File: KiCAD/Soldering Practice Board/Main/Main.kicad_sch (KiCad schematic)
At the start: 1 part, among them U1 STM32C071R8Tx

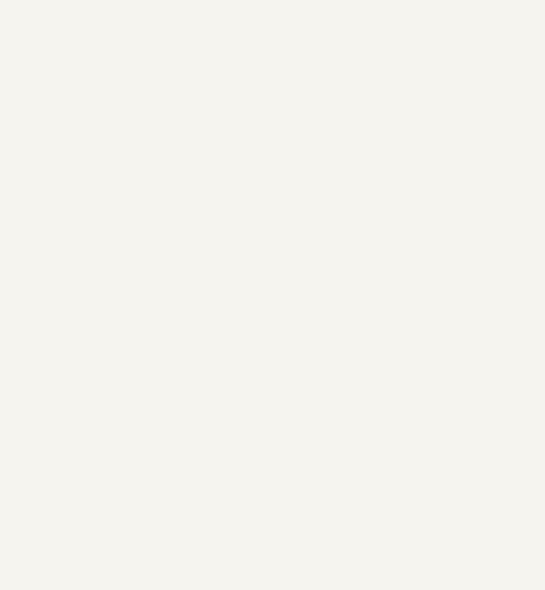
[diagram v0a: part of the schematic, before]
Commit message: Write BMi260 explanations
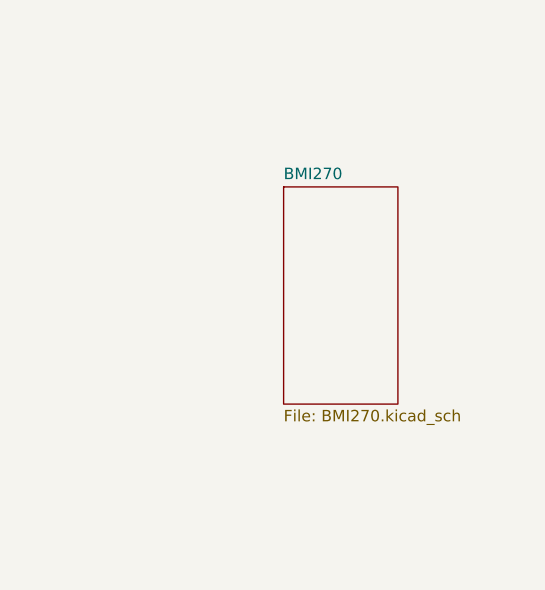
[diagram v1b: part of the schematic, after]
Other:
- added sheet BMI270 (BMI270.kicad_sch)
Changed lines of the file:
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@@
+		)
+	)
+	(sheet
+		(at 163.83 77.47)
+		(size 12.7 24.13)
+		(exclude_from_sim no)
+		(in_bom yes)
+		(on_board yes)
+		(dnp no)
+		(fields_autoplaced yes)
+		(stroke
+			(width 0.1524)
+			(type solid)
+		)
+		(fill
+			(color 0 0 0 0.0000)
+		)
+		(property "Sheetname" "BMI270"
+			(at 163.83 76.7584 0)
+			(effects
+				(font
+					(size 1.27 1.27)
+				)
+				(justify left bottom)
+			)
+		)
+		(property "Sheetfile" "BMI270.kicad_sch"
+			(at 163.83 102.1846 0)
+			(effects
+				(font
+					(size 1.27 1.27)
+				)
+				(justify left top)
+			)
+		)
+		(instances
+			(project "Main"
+				(path "/4f1abb7e-5ebf-459c-b427-2e7d0c6488f6"
+					(page "2")
+				)
+			)
 		)
 	)

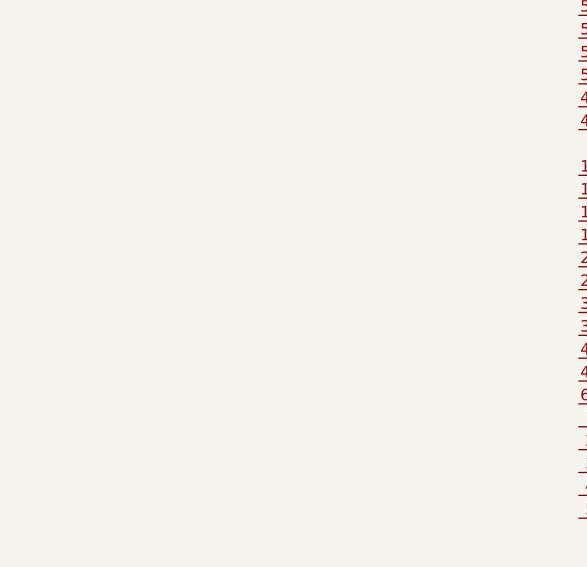
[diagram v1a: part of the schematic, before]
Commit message: create lsm spi schematic for practice board
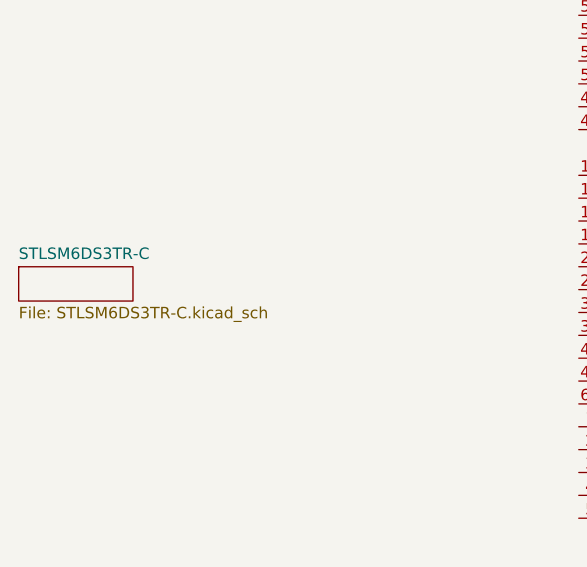
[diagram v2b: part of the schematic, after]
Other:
- added sheet STLSM6DS3TR-C (STLSM6DS3TR-C.kicad_sch)
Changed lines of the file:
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@@
+		)
+	)
+	(sheet
+		(at 43.18 111.76)
+		(size 12.7 3.81)
+		(exclude_from_sim no)
+		(in_bom yes)
+		(on_board yes)
+		(dnp no)
+		(fields_autoplaced yes)
+		(stroke
+			(width 0.1524)
+			(type solid)
+		)
+		(fill
+			(color 0 0 0 0.0000)
+		)
+		(property "Sheetname" "STLSM6DS3TR-C"
+			(at 43.18 111.0484 0)
+			(effects
+				(font
+					(size 1.27 1.27)
+				)
+				(justify left bottom)
+			)
+		)
+		(property "Sheetfile" "STLSM6DS3TR-C.kicad_sch"
+			(at 43.18 116.1546 0)
+			(effects
+				(font
+					(size 1.27 1.27)
+				)
+				(justify left top)
+			)
+		)
+		(instances
+			(project "Main"
+				(path "/4f1abb7e-5ebf-459c-b427-2e7d0c6488f6"
+					(page "3")
+				)
+			)
 		)
 	)

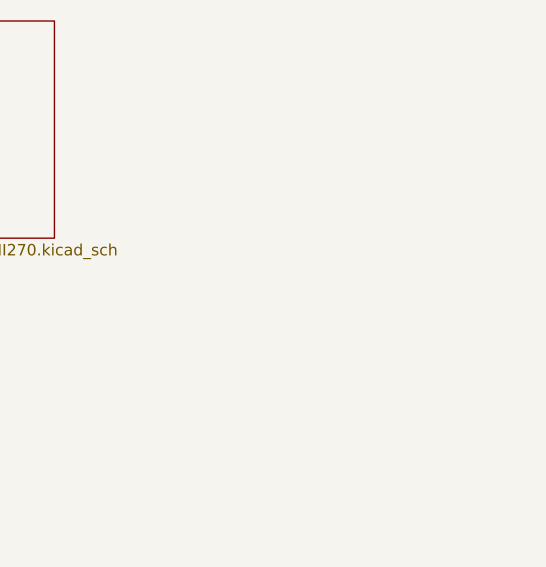
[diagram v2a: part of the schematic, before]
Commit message: Add BMP schematic
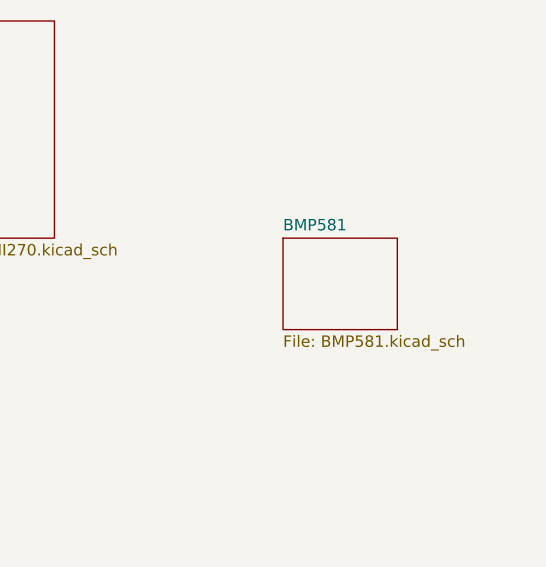
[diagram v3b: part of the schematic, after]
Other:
- added sheet BMP581 (BMP581.kicad_sch)
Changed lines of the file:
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@@
+	)
+	(sheet
+		(at 201.93 101.6)
+		(size 12.7 10.16)
+		(exclude_from_sim no)
+		(in_bom yes)
+		(on_board yes)
+		(dnp no)
+		(fields_autoplaced yes)
+		(stroke
+			(width 0.1524)
+			(type solid)
+		)
+		(fill
+			(color 0 0 0 0.0000)
+		)
+		(property "Sheetname" "BMP581"
+			(at 201.93 100.8884 0)
+			(effects
+				(font
+					(size 1.27 1.27)
+				)
+				(justify left bottom)
+			)
+		)
+		(property "Sheetfile" "BMP581.kicad_sch"
+			(at 201.93 112.3446 0)
+			(effects
+				(font
+					(size 1.27 1.27)
+				)
+				(justify left top)
+			)
+		)
+		(instances
+			(project "Main"
+				(path "/4f1abb7e-5ebf-459c-b427-2e7d0c6488f6"
+					(page "5")
+				)
+			)
+		)
 	)
 	(sheet

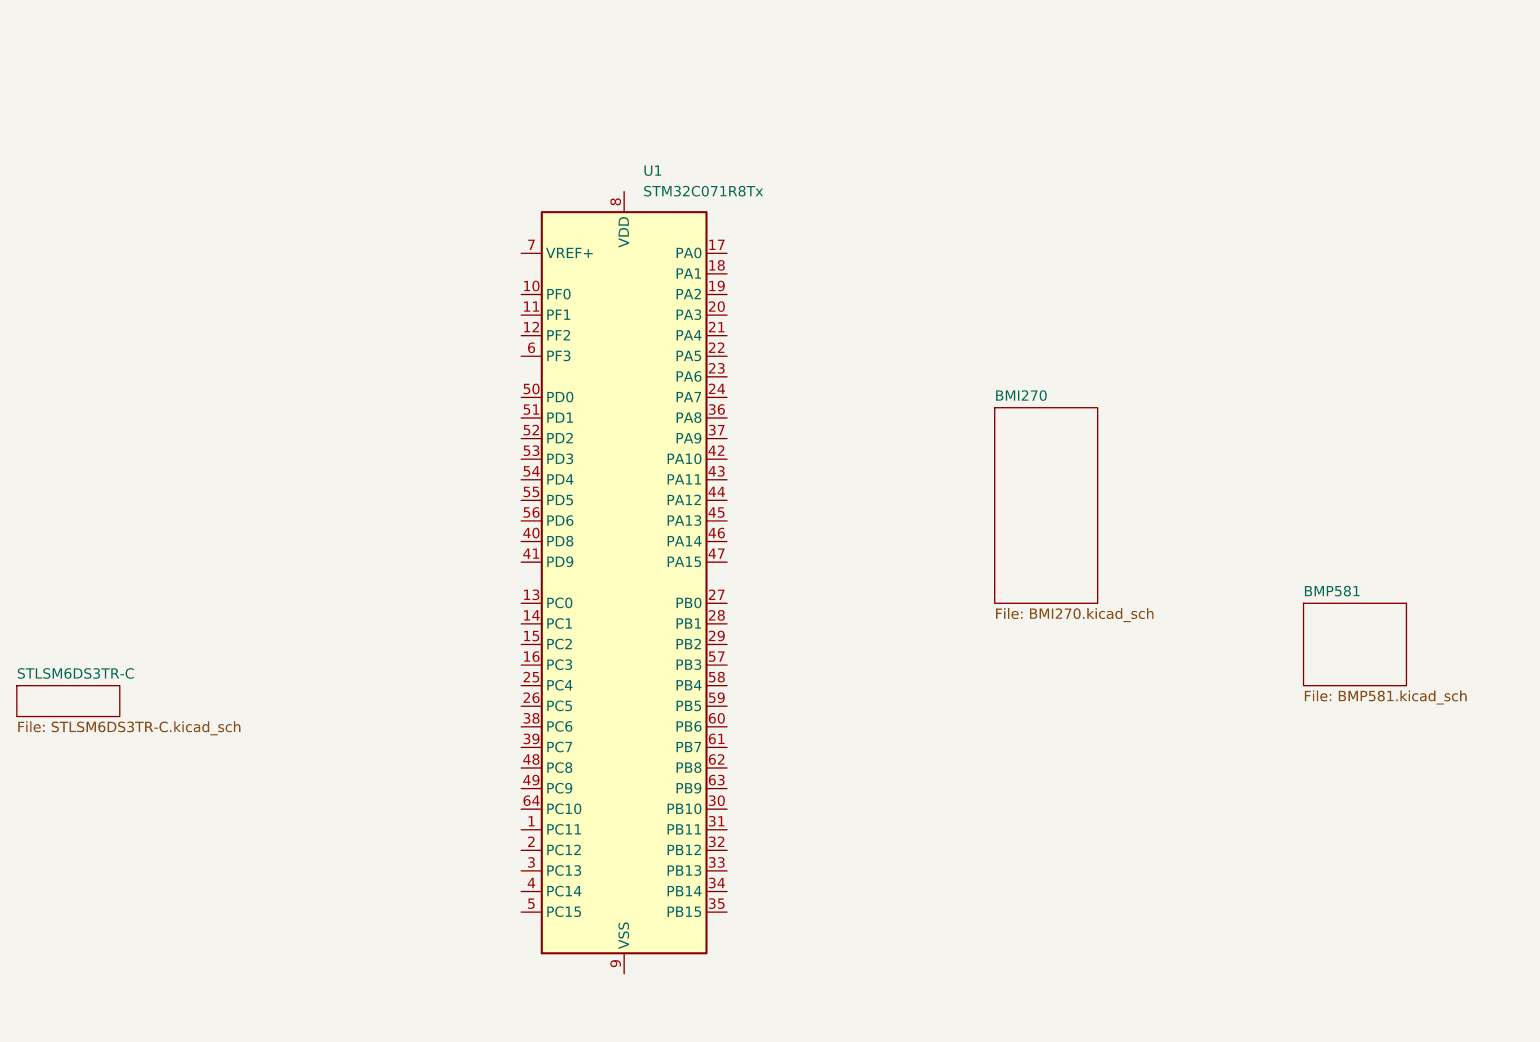
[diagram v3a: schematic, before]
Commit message: Configure IOC file, rename pins
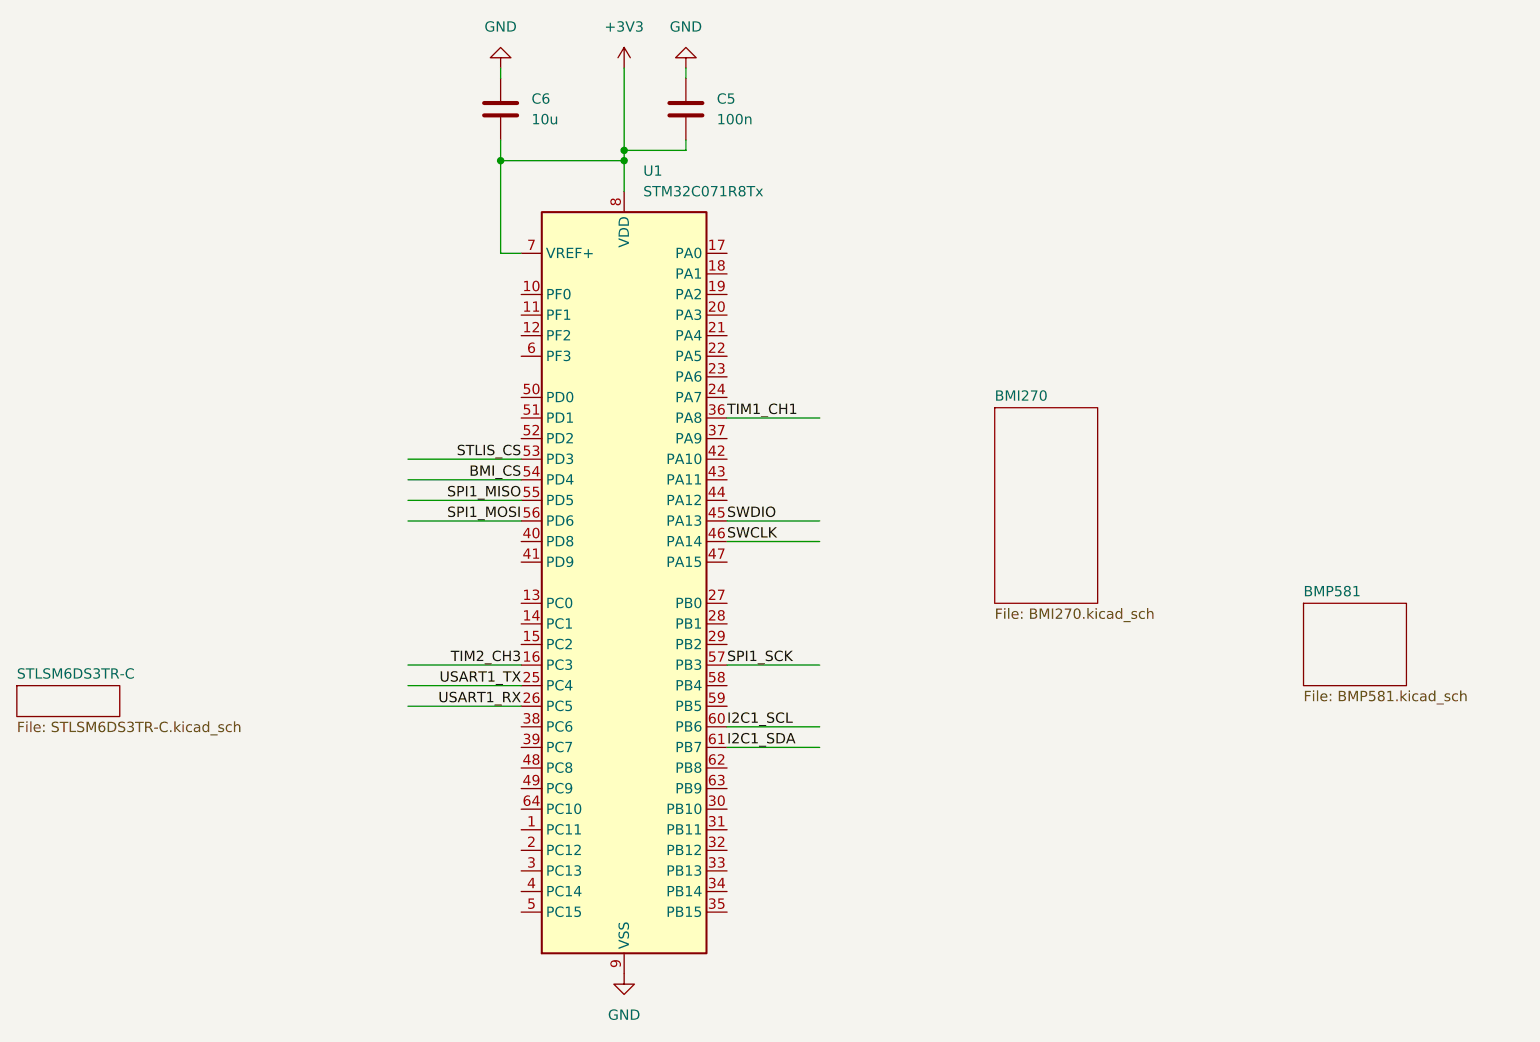
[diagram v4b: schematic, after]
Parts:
- added C5: 100n, symbol Device:C
- added C6: 10u, symbol Device:C
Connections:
- net TIM2_CH3: now reaches U1.16 (PC3)
- net USART1_TX: now reaches U1.25 (PC4)
- net USART1_RX: now reaches U1.26 (PC5)
- net TIM1_CH1: now reaches U1.36 (PA8)
- net SWDIO: now reaches U1.45 (PA13)
- net SWCLK: now reaches U1.46 (PA14)
- net STLIS_CS: now reaches U1.53 (PD3)
- net BMI_CS: now reaches U1.54 (PD4)
- net SPI1_MISO: now reaches U1.55 (PD5)
- net SPI1_MOSI: now reaches U1.56 (PD6)
- net SPI1_SCK: now reaches U1.57 (PB3)
- net I2C1_SCL: now reaches U1.60 (PB6)
- net I2C1_SDA: now reaches U1.61 (PB7)
- net +3V3: now reaches U1.7 (VREF+)
- net +3V3: now also U1.8 (VDD), C5.2, C6.2
- net GND: now reaches U1.9 (VSS)
- net GND: now also C5.1, C6.1

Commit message: Define more mcu pins
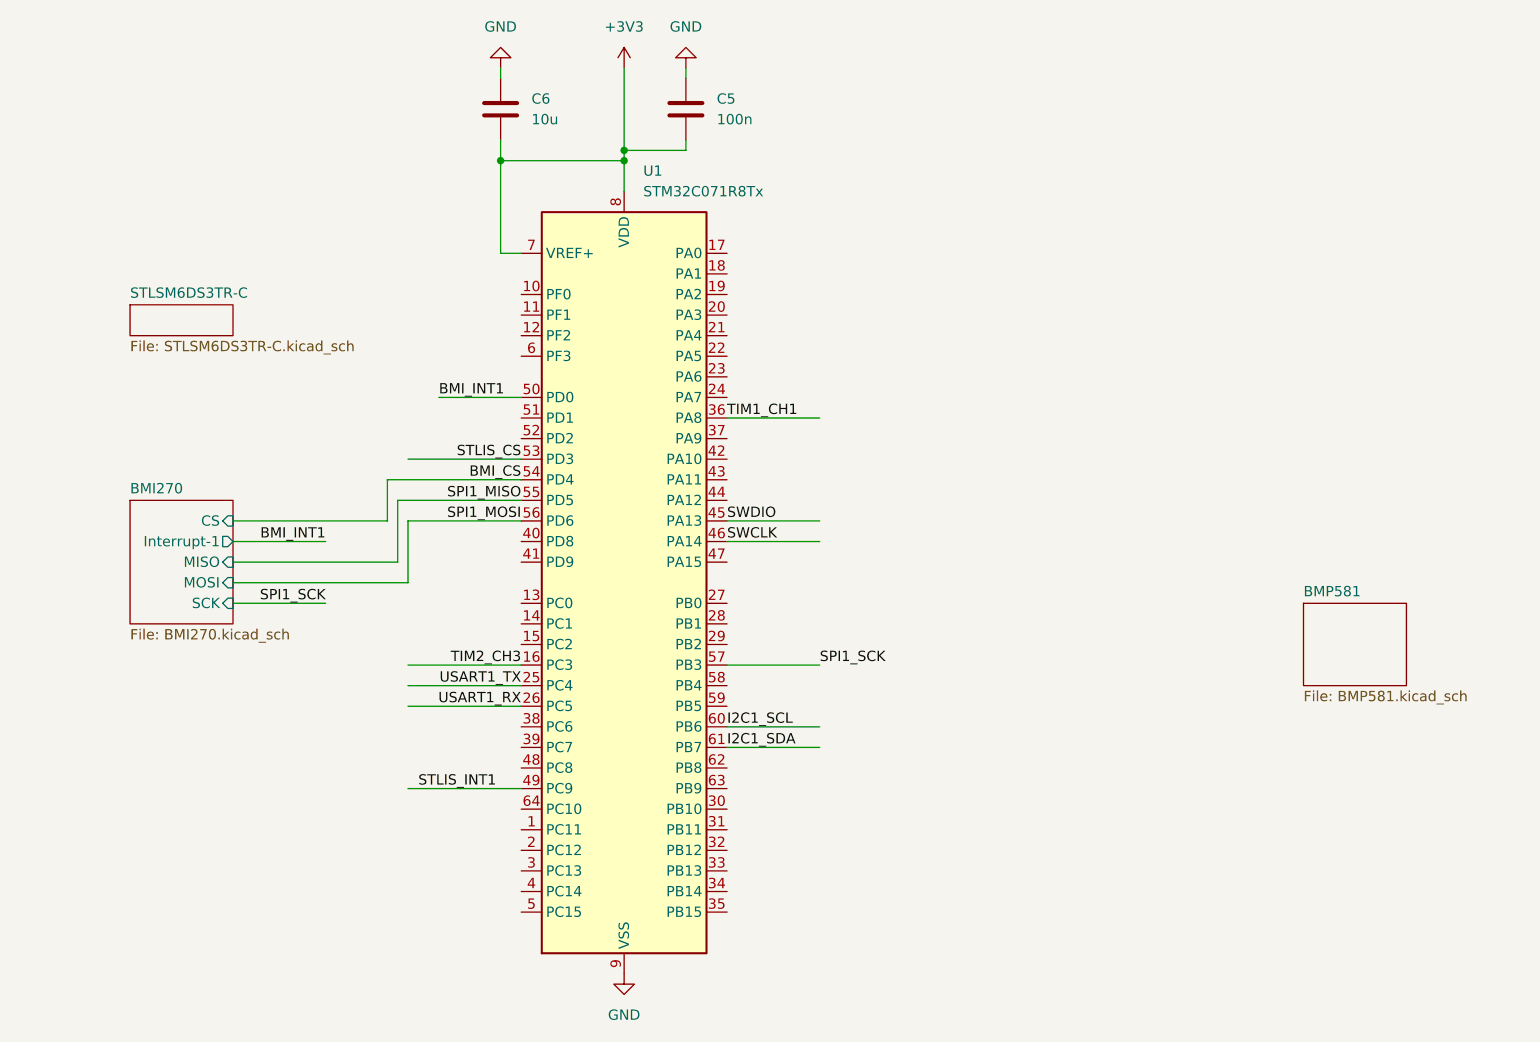
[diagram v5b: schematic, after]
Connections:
- net STLIS_INT1: now reaches U1.49 (PC9)
- net BMI_INT1: now reaches U1.50 (PD0)
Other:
- sheet BMI270 ports: added CS, Interrupt-1, MISO, MOSI, SCK; removed none
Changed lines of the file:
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@@
+	(wire
+		(pts
+			(xy 91.44 99.06) (xy 91.44 91.44)
+		)
+		(stroke
+			(width 0)
+			(type default)
+		)
+	)
+	(wire
+		(pts
+			(xy 91.44 124.46) (xy 105.41 124.46)
+		)
+		(stroke
+			(width 0)
+			(type default)
+		)
+	)
+	(wire
+		(pts
+			(xy 88.9 91.44) (xy 88.9 86.36)
+		)
+		(stroke
+			(width 0)
+			(type default)
+		)
+	)
 	(wire
 		(pts
@@
 	(wire
 		(pts
+			(xy 90.17 88.9) (xy 90.17 96.52)
+		)
+		(stroke
+			(width 0)
+			(type default)
+		)
+	)
+	(wire
+		(pts
+			(xy 69.85 93.98) (xy 81.28 93.98)
+		)
+		(stroke
+			(width 0)
+			(type default)
+		)
+	)
+	(wire
+		(pts
 			(xy 91.44 83.82) (xy 105.41 83.82)
 		)
@@
 	(wire
 		(pts
+			(xy 69.85 91.44) (xy 88.9 91.44)
+		)
+		(stroke
+			(width 0)
+			(type default)
+		)
+	)
+	(wire
+		(pts
 			(xy 130.81 119.38) (xy 142.24 119.38)
 		)
@@
 	(wire
 		(pts
-			(xy 91.44 86.36) (xy 105.41 86.36)
+			(xy 88.9 86.36) (xy 105.41 86.36)
+		)
+		(stroke
+			(width 0)
+			(type default)
+		)
+	)
+	(wire
+		(pts
+			(xy 69.85 101.6) (xy 81.28 101.6)
+		)
+		(stroke
+			(width 0)
+			(type default)
+		)
+	)
+	(wire
+		(pts
+			(xy 90.17 88.9) (xy 105.41 88.9)
 		)
 		(stroke
@@
 	(wire
 		(pts
+			(xy 69.85 99.06) (xy 91.44 99.06)
+		)
+		(stroke
+			(width 0)
+			(type default)
+		)
+	)
+	(wire
+		(pts
+			(xy 95.25 76.2) (xy 105.41 76.2)
+		)
+		(stroke
+			(width 0)
+			(type default)
+		)
+	)
+	(wire
+		(pts
 			(xy 125.73 45.72) (xy 118.11 45.72)
 		)
@@
 	(wire
 		(pts
+			(xy 90.17 96.52) (xy 69.85 96.52)
+		)
+		(stroke
+			(width 0)
+			(type default)
+		)
+	)
+	(wire
+		(pts
 			(xy 102.87 46.99) (xy 102.87 58.42)
 		)
@@
 	(wire
 		(pts
-			(xy 130.81 109.22) (xy 142.24 109.22)
-		)
-		(stroke
-			(width 0)
-			(type default)
-		)
-	)
-	(wire
-		(pts
 			(xy 118.11 46.99) (xy 118.11 50.8)
 		)
@@
 	(wire
 		(pts
+			(xy 142.24 109.22) (xy 130.81 109.22)
+		)
+		(stroke
+			(width 0)
+			(type default)
+		)
+	)
+	(wire
+		(pts
 			(xy 102.87 58.42) (xy 105.41 58.42)
-		)
-		(stroke
-			(width 0)
-			(type default)
-		)
-	)
-	(wire
-		(pts
-			(xy 91.44 88.9) (xy 105.41 88.9)
 		)
 		(stroke
@@
 	)
 	(label "SPI1_SCK"
-		(at 130.81 109.22 0)
+		(at 142.24 109.22 0)
 		(effects
 			(font
@@
 		)
 	)
+	(label "STLIS_INT1"
+		(at 92.71 124.46 0)
+		(effects
+			(font
+				(size 1.27 1.27)
+			)
+			(justify left bottom)
+		)
+	)
+	(label "SPI1_SCK"
+		(at 81.28 101.6 180)
+		(effects
+			(font
+				(size 1.27 1.27)
+			)
+			(justify right bottom)
+		)
+	)
 	(label "BMI_CS"
 		(at 105.41 86.36 180)
@@
 		)
 	)
+	(label "BMI_INT1"
+		(at 95.25 76.2 0)
+		(effects
+			(font
+				(size 1.27 1.27)
+			)
+			(justify left bottom)
+		)
+	)
 	(label "SPI1_MISO"
 		(at 105.41 88.9 180)
@@
 			)
 			(justify left bottom)
+		)
+	)
+	(label "BMI_INT1"
+		(at 81.28 93.98 180)
+		(effects
+			(font
+				(size 1.27 1.27)
+			)
+			(justify right bottom)
 		)
 	)
@@
 	)
 	(sheet
-		(at 163.83 77.47)
-		(size 12.7 24.13)
+		(at 57.15 88.9)
+		(size 12.7 15.24)
 		(exclude_from_sim no)
 		(in_bom yes)
@@
 		)
 		(property "Sheetname" "BMI270"
-			(at 163.83 76.7584 0)
+			(at 57.15 88.1884 0)
 			(effects
 				(font
@@
 		)
 		(property "Sheetfile" "BMI270.kicad_sch"
-			(at 163.83 102.1846 0)
+			(at 57.15 104.7246 0)
 			(effects
 				(font
@@
 				)
 				(justify left top)
+			)
+		)
+		(pin "CS" input
+			(at 69.85 91.44 0)
+			(effects
+				(font
+					(size 1.27 1.27)
+				)
+				(justify right)
+			)
+		)
+		(pin "Interrupt-1" output
+			(at 69.85 93.98 0)
+			(effects
+				(font
+					(size 1.27 1.27)
+				)
+				(justify right)
+			)
+		)
+		(pin "MISO" input
+			(at 69.85 96.52 0)
+			(effects
+				(font
+					(size 1.27 1.27)
+				)
+				(justify right)
+			)
+		)
+		(pin "MOSI" input
+			(at 69.85 99.06 0)
+			(effects
+				(font
+					(size 1.27 1.27)
+				)
+				(justify right)
+			)
+		)
+		(pin "SCK" input
+			(at 69.85 101.6 0)
+			(effects
+				(font
+					(size 1.27 1.27)
+				)
+				(justify right)
 			)
 		)
@@
 	)
 	(sheet
-		(at 43.18 111.76)
+		(at 57.15 64.77)
 		(size 12.7 3.81)
 		(exclude_from_sim no)
@@
 		)
 		(property "Sheetname" "STLSM6DS3TR-C"
-			(at 43.18 111.0484 0)
+			(at 57.15 64.0584 0)
 			(effects
 				(font
@@
 		)
 		(property "Sheetfile" "STLSM6DS3TR-C.kicad_sch"
-			(at 43.18 116.1546 0)
-			(effects
-				(font
+			(at 57.15 69.1646 0)
+			(effects
+				(font
